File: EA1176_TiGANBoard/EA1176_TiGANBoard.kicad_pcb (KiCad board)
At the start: 2 copper layers, 127 x 88.9 mm, 11 parts, among them J1 Conn_01x04_Male, J2 L829-1J1T-43, J4 Conn_ARM_JTAG_SWD_10, Q1 BSS138PW, Q2 BSS138PW, U1 iMXRT1176uCOM, U2 BOOSTXL_3PhGaNInv_noTerminalB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

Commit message: [fix] CADを更新 V1.0 beta
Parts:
- added C2: 0.1u, Capacitor_SMD:C_0402_1005Metric, F.Cu at (-44.7, -25.1)
- added C3: 0.1u, Capacitor_SMD:C_0402_1005Metric, F.Cu at (-36.3, -29.2)
- added C4: 1u, Capacitor_SMD:C_0402_1005Metric, F.Cu at (-35.3, -29.2)
- added C5: 0.1u, Capacitor_SMD:C_0402_1005Metric, F.Cu at (-32.4, -24.3)
- added D1: RB521S30T1G, Diode_SMD:D_SOD-523, F.Cu at (14.0, -59.7)
- added D2: PESD5V0L5UV, Package_TO_SOT_SMD:SOT-666, F.Cu at (9.40, -34.4)
- added D3: PESD5V0L5UV, Package_TO_SOT_SMD:SOT-666, F.Cu at (-43.4, -30.0)
- added J3: Conn_01x03, Connector_PinHeader_2.54mm:PinHeader_1x03_P2.54mm_Vertical, F.Cu at (-45.7, -34.3)
- added J5: Conn_01x04, Connector_JST:JST_XH_B4B-XH-A_1x04_P2.50mm_Vertical, F.Cu at (-36.1, -19.9)
- added J6: Conn_01x04, Connector_PinHeader_2.54mm:PinHeader_1x04_P2.54mm_Vertical, F.Cu at (-66.0, -24.9)
- added R10: 50, Resistor_SMD:R_0402_1005Metric, F.Cu at (14.4, -56.1)
- added R11: 50, Resistor_SMD:R_0402_1005Metric, F.Cu at (14.4, -54.1)
- added R12: 50, Resistor_SMD:R_0402_1005Metric, F.Cu at (14.4, -55.1)
- added R13: 1k, Resistor_SMD:R_0402_1005Metric, F.Cu at (14.4, -53.1)
- added R4: 10k, Resistor_SMD:R_0402_1005Metric, F.Cu at (-40.4, -26.7)
- added R5: 100, Resistor_SMD:R_0402_1005Metric, F.Cu at (-42.4, -25.6)
- added R6: 60, Resistor_SMD:R_0402_1005Metric, F.Cu at (-31.0, -25.7)
- added R7: 60, Resistor_SMD:R_0402_1005Metric, F.Cu at (-33.8, -25.7)
- added R8: 10k, Resistor_SMD:R_0402_1005Metric, F.Cu at (12.6, -58.7)
- added R9: 50, Resistor_SMD:R_0402_1005Metric, F.Cu at (14.4, -57.1)
- added SW1: SW_MEC_5E, Button_Switch_THT:SW_TH_Tactile_Omron_B3F-10xx, F.Cu at (-49.0, -21.8)
- added TP1: TestPoint, Connector_PinHeader_2.54mm:PinHeader_1x01_P2.54mm_Vertical, F.Cu at (-66.0, -19.8)
- added TP2: TestPoint, Connector_PinHeader_2.54mm:PinHeader_1x01_P2.54mm_Vertical, F.Cu at (-61.0, -19.8)
- added TP3: TestPoint, Connector_PinHeader_2.54mm:PinHeader_1x01_P2.54mm_Vertical, F.Cu at (-63.5, -19.8)
- added TP4: TestPoint, Connector_PinHeader_2.54mm:PinHeader_1x01_P2.54mm_Vertical, F.Cu at (-58.4, -19.8)
- added U3: TCAN332G, Package_TO_SOT_SMD:SOT-23-8, F.Cu at (-32.4, -29.3)
- J1: value Conn_01x04_Male -> Conn_01x03; footprint Connector_PinHeader_2.54mm:PinHeader_1x04_P2.54mm_Vertical -> Connector_PinHeader_2.54mm:PinHeader_1x03_P2.54mm_Vertical
- moved J1 150.1 mm to (-63.5, -34.3), turned to 90 degrees
- moved C1 145.6 mm to (6.35, -36.4), turned to 90 degrees
- moved J2 144.8 mm to (-6.10, -26.7)
- moved Q1 143.3 mm to (-22.9, -17.8)
- moved Q2 143.3 mm to (-22.9, -22.9)
- moved R1 143.3 mm to (-19.1, -17.8)
- moved R2 143.3 mm to (-19.1, -22.9)
- moved R3 141.6 mm to (6.60, -18.3)
- moved U1 140.9 mm to (-13.3, -68.1), turned to 90 degrees
- moved U2 140.8 mm to (-27.9, -68.6)
- moved J4 112.6 mm to (10.4, -27.9)
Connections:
- net Net-(U1-Pad89) renamed /CAN1_EXT_TICK
- J1 pad 1: /USER_GPIO -> +3V3
- J1 pad 3: /ADC_U1 -> GND
- J2 pad 16: /EA1176_SOM/PERI_3V3 -> +3V3
- J4 pad 10: /EA1176_SOM/JTAG_TRST -> /EA1176_SOM/Conn_RST
- J4 pad 2: /EA1176_SOM/JTAG_TMS -> /EA1176_SOM/Conn_TMS
- J4 pad 4: /EA1176_SOM/JTAG_TCK -> /EA1176_SOM/Conn_TCK
- J4 pad 6: /EA1176_SOM/JTAG_TDO -> /EA1176_SOM/Conn_TDO
- J4 pad 8: /EA1176_SOM/JTAG_TDI -> /EA1176_SOM/Conn_TDI
- U1 pad 105: /EA1176_SOM/ADC2_B6 -> /UART_RX
- U1 pad 107: /EA1176_SOM/ADC2_A6 -> /UART_TX
- U1 pad 142: Net-(U1-Pad142) -> /USER_SW
- U1 pad 170: Net-(U1-Pad170) -> /EA1176_SOM/POR_B
- U1 pad 20: /3V3 -> +3V3
- U1 pad 22: /3V3 -> +3V3
- U1 pad 24: /3V3 -> +3V3
- U1 pad 26: /3V3 -> +3V3
- U1 pad 28: /3V3 -> +3V3
- U1 pad 30: /3V3 -> +3V3
- U1 pad 93: Net-(U1-Pad93) -> /CAN1_TX
- U1 pad 95: Net-(U1-Pad95) -> /CAN1_RX
- U2 pad 1: /3V3 -> +3V3
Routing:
- net +3V3: track 0.00 -> 188.5 mm, vias 0 -> 4
- net GND: track 0.00 -> 125.7 mm, vias 0 -> 201
- net /UART_RX: track 0.00 -> 100.9 mm, vias 0 -> 2
- net /UART_TX: track 0.00 -> 97.4 mm, vias 0 -> 2
- net /PWM_TRIG: track 0.00 -> 96.5 mm, vias 0 -> 4
- net /nEnable: track 0.00 -> 79.9 mm, vias 0 -> 2
- net /OT: track 0.00 -> 79.7 mm
- net /PWM_UH: track 0.00 -> 78.3 mm
- net /PWM_UL: track 0.00 -> 76.5 mm
- net /PWM_VH: track 0.00 -> 75.9 mm, vias 0 -> 2
- net /USER_SW: track 0.00 -> 75.6 mm, vias 0 -> 4
- net /EA1176_SOM/ETH1_LED_ACT: track 0.00 -> 74.6 mm
- net /PWM_VL: track 0.00 -> 72.9 mm, vias 0 -> 2
- net /ADC_U1: track 0.00 -> 70.1 mm, vias 0 -> 4
- net /PWM_WL: track 0.00 -> 69.1 mm
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- added copper zone on B.Cu, net GND
- added copper zone on F.Cu, net GND
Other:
- board size 127 x 88.9 mm -> 96.5 x 97.8 mm
- copper layers 2 -> 4
- net class Default: clearance 0.2 -> 0.127; trace_width 0.25 -> 0.127; via_dia 0.8 -> 0.6; via_drill 0.4 -> 0.3
- rule trace_clearance: 0.2 -> 0.127
- rule trace_min: 0.2 -> 0.127
- rule via_min_size: 0.4 -> 0.6

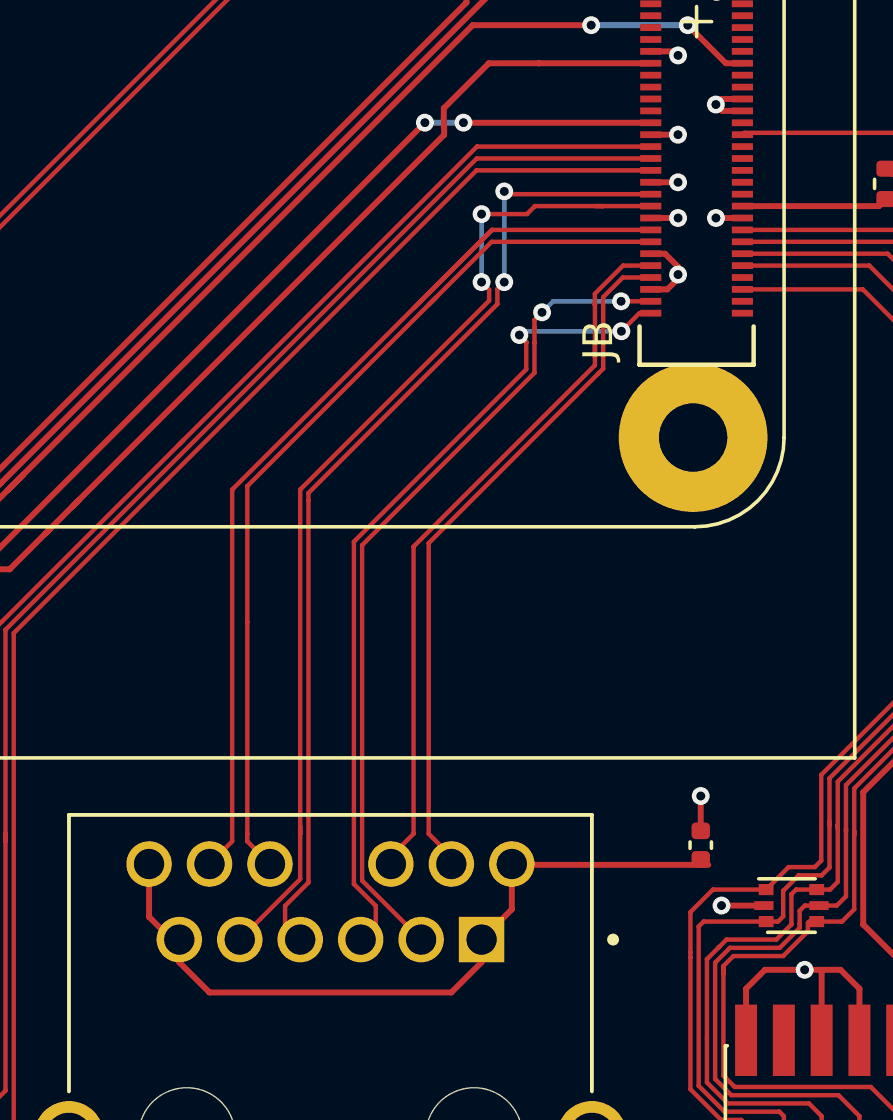
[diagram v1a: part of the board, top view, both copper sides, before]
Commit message: [fix]RJ45のうねうねを追加
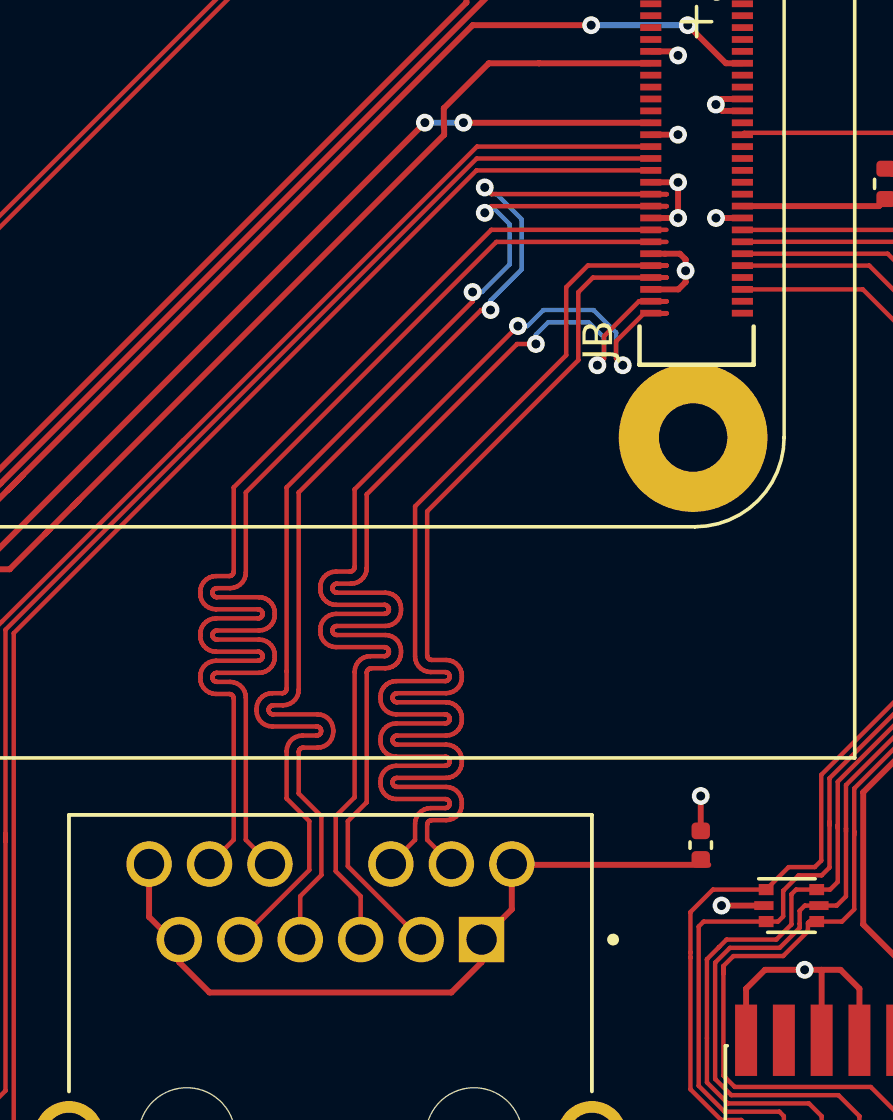
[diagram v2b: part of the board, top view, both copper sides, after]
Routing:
- net /EA1176_SOM/ETH1_TRXP3: track 23.7 -> 39.6 mm
- net /EA1176_SOM/ETH1_TRXN3: track 24.9 -> 40.3 mm
- net /EA1176_SOM/ETH1_TRXP2: track 28.3 -> 40.5 mm
- net /EA1176_SOM/ETH1_TRXN2: track 28.2 -> 40.0 mm
- net /EA1176_SOM/ETH1_TRXN0: track 30.3 -> 39.3 mm
- net /EA1176_SOM/ETH1_TRXP1: track 33.4 -> 40.6 mm
- net /EA1176_SOM/ETH1_TRXN1: track 34.3 -> 40.0 mm
- net /EA1176_SOM/ETH1_TRXP0: track 34.3 -> 40.0 mm
- net GND: track 125.7 -> 127.6 mm

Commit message: [fix] logo/Gerber
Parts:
- added G***: LOGO, footprint:digitalservo_logo, F.Cu at (10.4, -22.0)
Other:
- board text added: "Rev. 1.0"
